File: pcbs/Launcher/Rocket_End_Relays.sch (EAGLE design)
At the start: 40 parts, among them IC2 LM2576T-ADJ, K4 LD105, K5 LD105, K6 LD105, K7 LD105, T1 BC547, T2 BC547, T3 BC547, T4 BC547, T5 BC547, U1 ARDUINO-MEGAPRO-5V, X1 1751248, X2 22-23-2041, X3 22-23-2021, X4 1751248, X5 22-23-2021

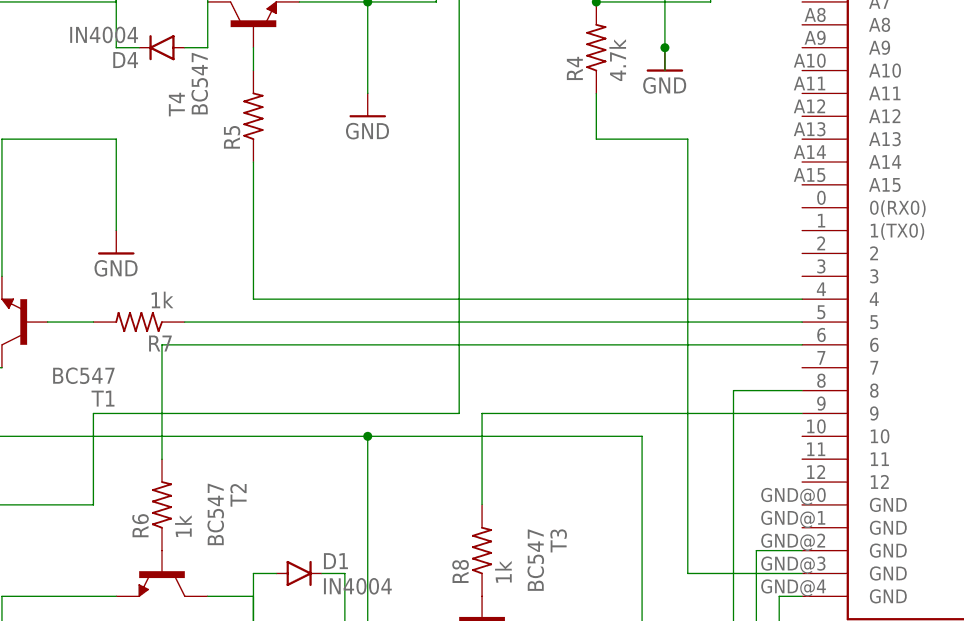
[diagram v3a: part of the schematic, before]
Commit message: * Moving across pins, so we don't use pin 4. Pin 4 is used by SDCARD CS.
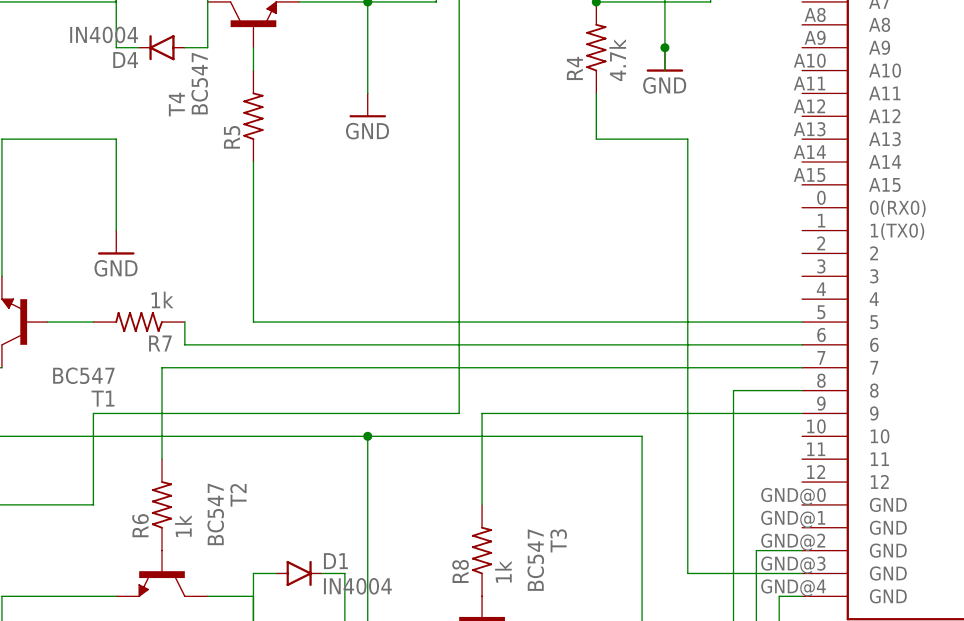
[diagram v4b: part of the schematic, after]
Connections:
- net N$4: now also U1.5; no longer U1.4
- net N$8: now also U1.6; no longer U1.5
- net N$9: now also U1.7; no longer U1.6
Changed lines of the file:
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@@
 <net name="N$4" class="0">
 <segment>
-<pinref part="U1" gate="G$1" pin="4"/>
-<wire x1="17.78" y1="35.56" x2="-43.18" y2="35.56" width="0.1524" layer="91"/>
-<wire x1="-43.18" y1="35.56" x2="-43.18" y2="50.8" width="0.1524" layer="91"/>
+<wire x1="-43.18" y1="33.02" x2="-43.18" y2="50.8" width="0.1524" layer="91"/>
 <pinref part="R5" gate="G$1" pin="1"/>
-</segment>
-</net>
-<net name="N$8" class="0">
-<segment>
 <pinref part="U1" gate="G$1" pin="5"/>
-<wire x1="17.78" y1="33.02" x2="-50.8" y2="33.02" width="0.1524" layer="91"/>
-<pinref part="R7" gate="G$1" pin="1"/>
+<wire x1="-43.18" y1="33.02" x2="17.78" y2="33.02" width="0.1524" layer="91"/>
 </segment>
 </net>
 <net name="N$9" class="0">
 <segment>
-<pinref part="U1" gate="G$1" pin="6"/>
-<wire x1="17.78" y1="30.48" x2="-53.34" y2="30.48" width="0.1524" layer="91"/>
-<wire x1="-53.34" y1="30.48" x2="-53.34" y2="17.78" width="0.1524" layer="91"/>
 <pinref part="R6" gate="G$1" pin="2"/>
+<pinref part="U1" gate="G$1" pin="7"/>
+<wire x1="-53.34" y1="27.94" x2="-53.34" y2="17.78" width="0.1524" layer="91"/>
+<wire x1="17.78" y1="27.94" x2="-53.34" y2="27.94" width="0.1524" layer="91"/>
 </segment>
 </net>
@@
 </segment>
 </net>
+<net name="N$8" class="0">
+<segment>
+<pinref part="R7" gate="G$1" pin="1"/>
+<wire x1="-50.8" y1="33.02" x2="-50.8" y2="30.48" width="0.1524" layer="91"/>
+<pinref part="U1" gate="G$1" pin="6"/>
+<wire x1="-50.8" y1="30.48" x2="17.78" y2="30.48" width="0.1524" layer="91"/>
+</segment>
+</net>

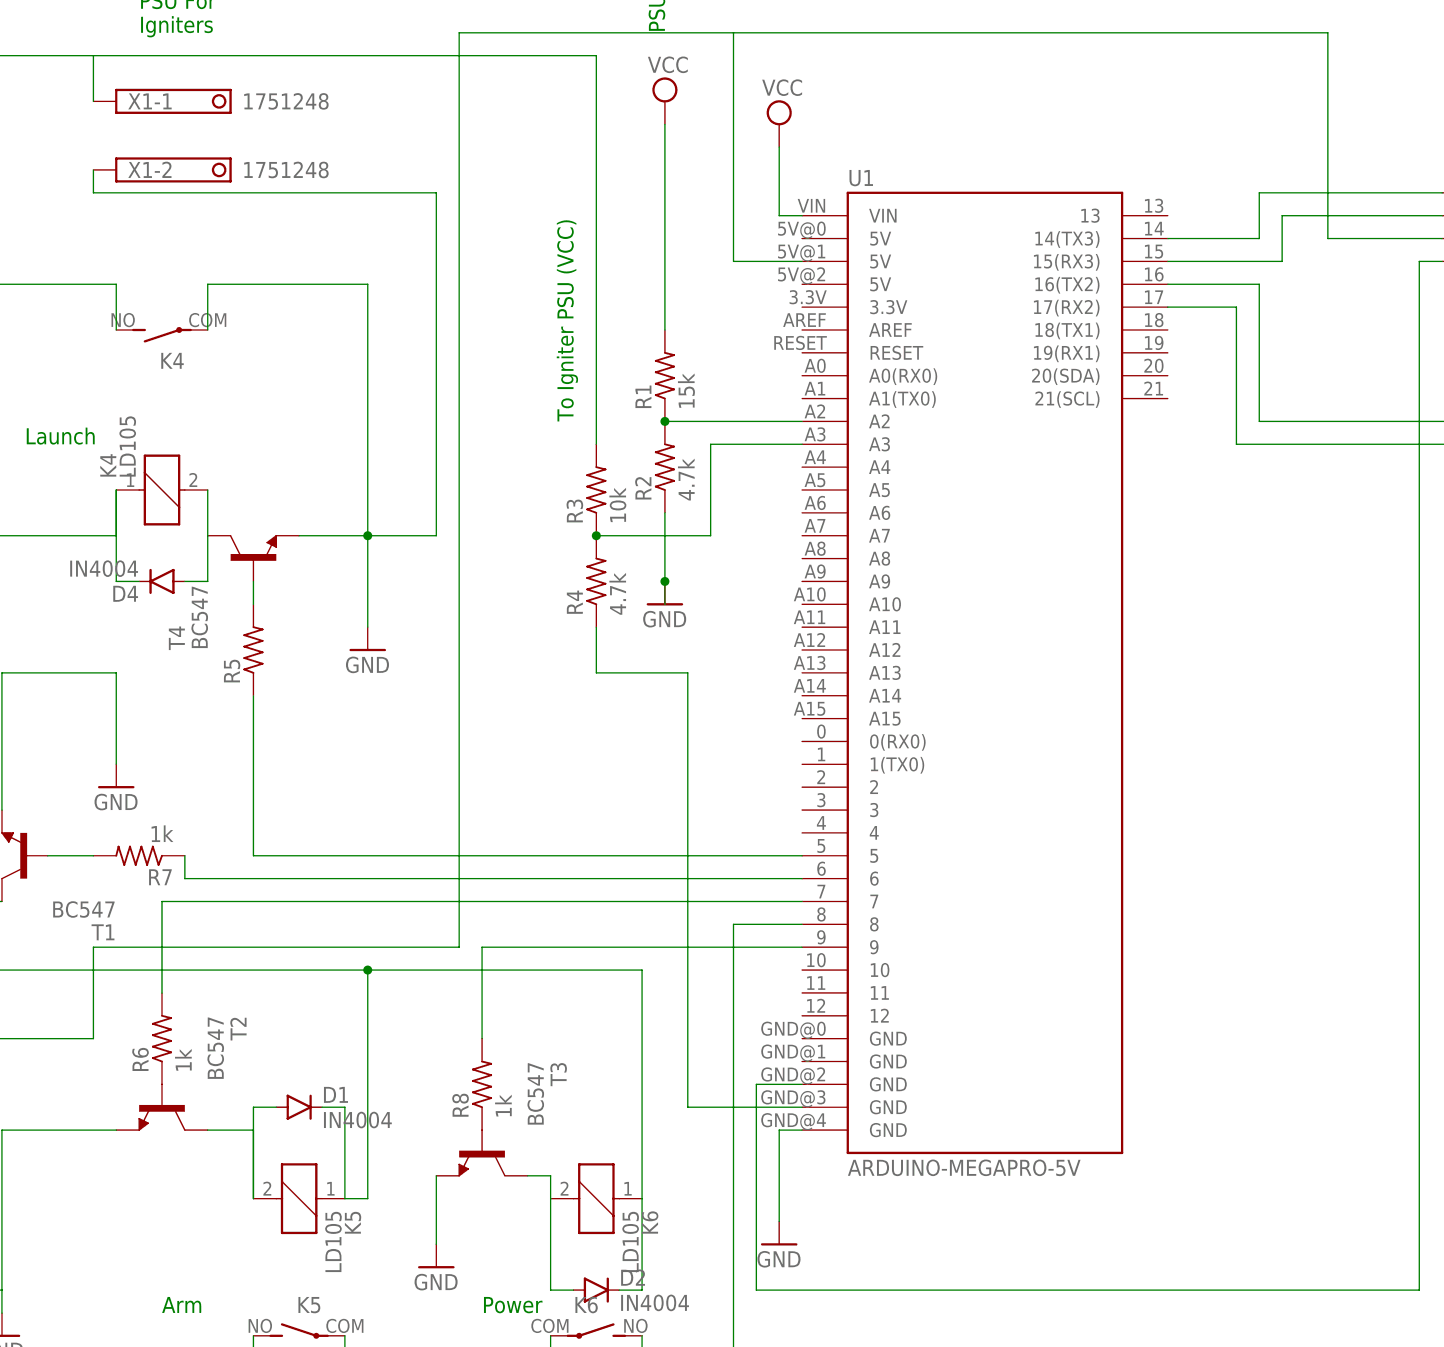
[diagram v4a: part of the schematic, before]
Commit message: * Re-route launch pin to pin 3 instead and keep all other pins as they were.
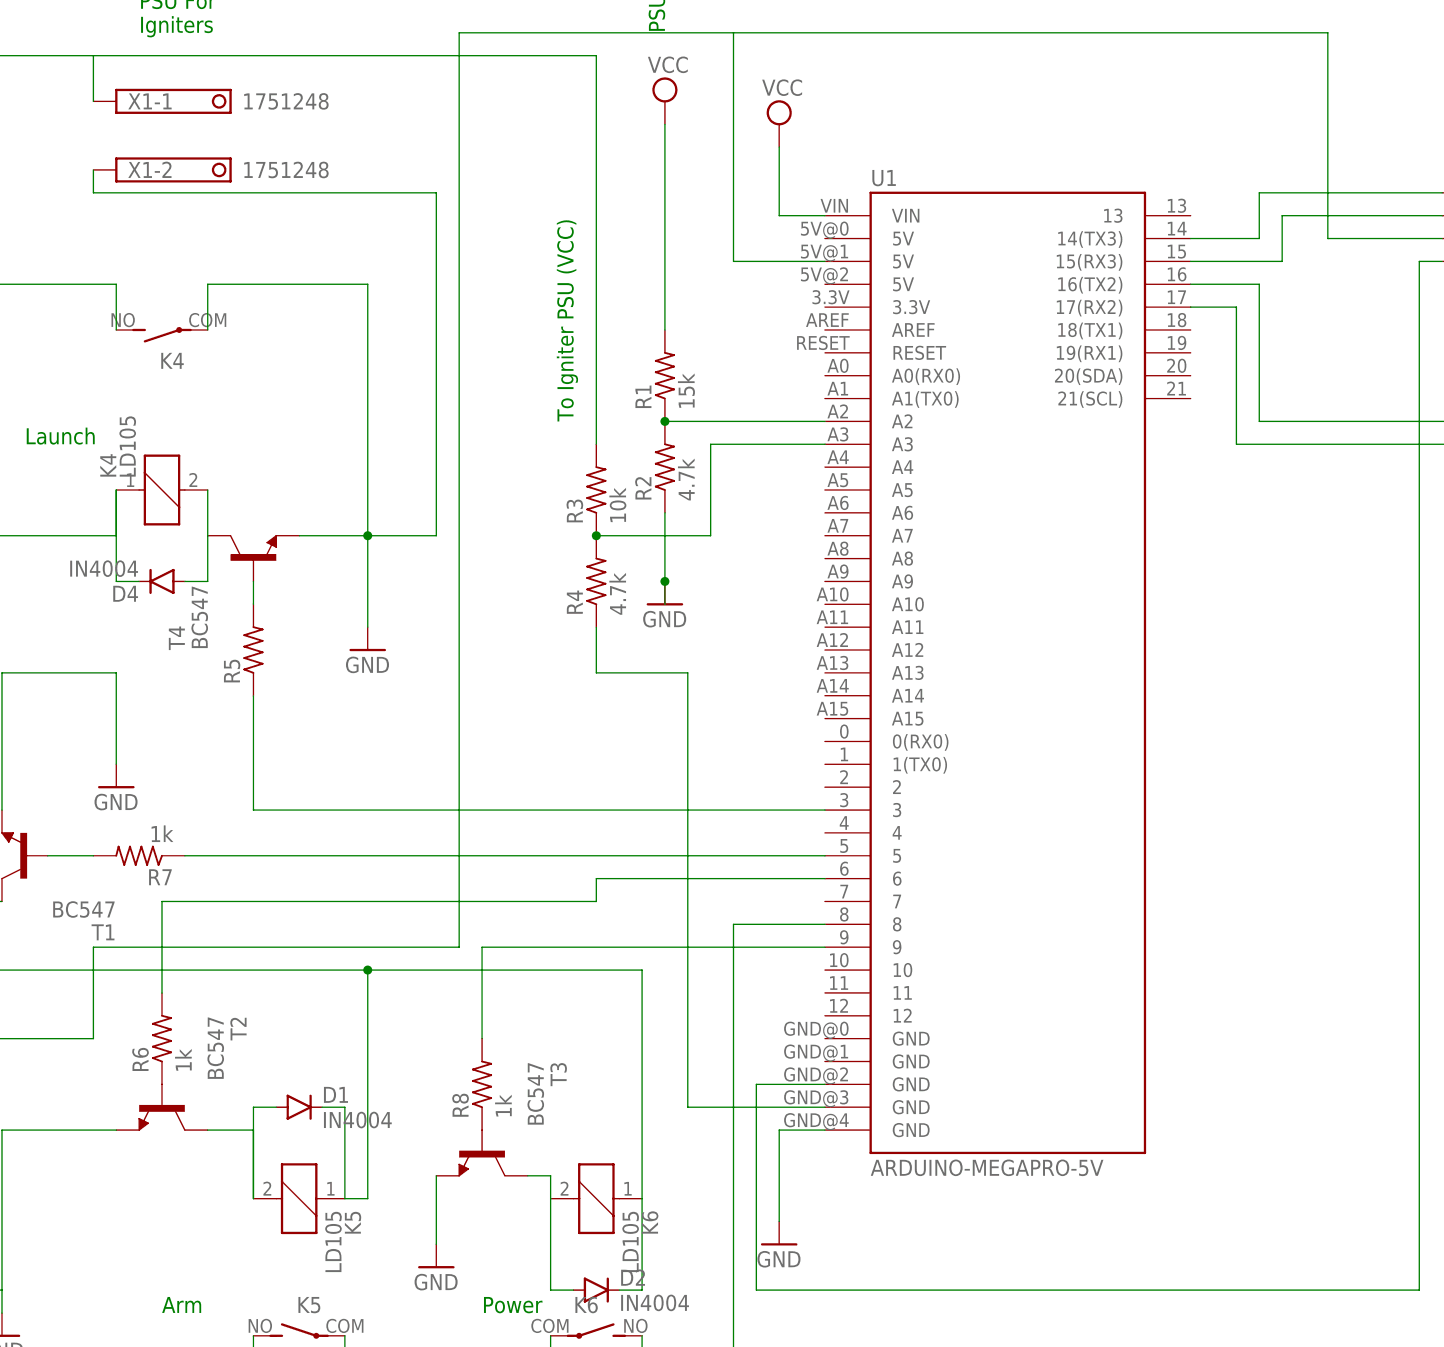
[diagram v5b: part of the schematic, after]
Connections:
- net N$4: now also R7.1; no longer R5.1
- net N$8: now also R5.1, U1.3; no longer R7.1, U1.6
- net N$9: now also U1.6; no longer U1.7
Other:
- moved on the sheet: U1
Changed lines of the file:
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@@
 </plain>
 <instances>
-<instance part="U1" gate="G$1" x="38.1" y="53.34"/>
+<instance part="U1" gate="G$1" x="40.64" y="53.34"/>
 <instance part="X2" gate="-1" x="91.44" y="106.68"/>
 <instance part="X2" gate="-2" x="91.44" y="104.14"/>
@@
 <pinref part="U1" gate="G$1" pin="14(TX3)"/>
 <wire x1="68.58" y1="106.68" x2="68.58" y2="101.6" width="0.1524" layer="91"/>
-<wire x1="68.58" y1="101.6" x2="58.42" y2="101.6" width="0.1524" layer="91"/>
+<wire x1="68.58" y1="101.6" x2="60.96" y2="101.6" width="0.1524" layer="91"/>
 </segment>
 </net>
@@
 <segment>
 <pinref part="U1" gate="G$1" pin="GND@4"/>
-<wire x1="17.78" y1="2.54" x2="15.24" y2="2.54" width="0.1524" layer="91"/>
+<wire x1="20.32" y1="2.54" x2="15.24" y2="2.54" width="0.1524" layer="91"/>
 <wire x1="15.24" y1="2.54" x2="15.24" y2="-7.62" width="0.1524" layer="91"/>
 <pinref part="GND10" gate="1" pin="GND"/>
@@
 <segment>
 <pinref part="U1" gate="G$1" pin="VIN"/>
-<wire x1="17.78" y1="104.14" x2="15.24" y2="104.14" width="0.1524" layer="91"/>
+<wire x1="20.32" y1="104.14" x2="15.24" y2="104.14" width="0.1524" layer="91"/>
 <wire x1="15.24" y1="104.14" x2="15.24" y2="111.76" width="0.1524" layer="91"/>
 <pinref part="SUPPLY3" gate="G$1" pin="VCC"/>
@@
 <segment>
 <pinref part="U1" gate="G$1" pin="A2"/>
-<wire x1="17.78" y1="81.28" x2="2.54" y2="81.28" width="0.1524" layer="91"/>
+<wire x1="20.32" y1="81.28" x2="2.54" y2="81.28" width="0.1524" layer="91"/>
 <pinref part="R1" gate="G$1" pin="1"/>
 <pinref part="R2" gate="G$1" pin="2"/>
@@
 <segment>
 <pinref part="U1" gate="G$1" pin="A3"/>
-<wire x1="17.78" y1="78.74" x2="7.62" y2="78.74" width="0.1524" layer="91"/>
+<wire x1="20.32" y1="78.74" x2="7.62" y2="78.74" width="0.1524" layer="91"/>
 <wire x1="7.62" y1="78.74" x2="7.62" y2="68.58" width="0.1524" layer="91"/>
 <wire x1="7.62" y1="68.58" x2="-5.08" y2="68.58" width="0.1524" layer="91"/>
@@
 </segment>
 </net>
-<net name="N$4" class="0">
-<segment>
-<wire x1="-43.18" y1="33.02" x2="-43.18" y2="50.8" width="0.1524" layer="91"/>
-<pinref part="R5" gate="G$1" pin="1"/>
-<pinref part="U1" gate="G$1" pin="5"/>
-<wire x1="-43.18" y1="33.02" x2="17.78" y2="33.02" width="0.1524" layer="91"/>
-</segment>
-</net>
 <net name="N$9" class="0">
 <segment>
 <pinref part="R6" gate="G$1" pin="2"/>
-<pinref part="U1" gate="G$1" pin="7"/>
 <wire x1="-53.34" y1="27.94" x2="-53.34" y2="17.78" width="0.1524" layer="91"/>
-<wire x1="17.78" y1="27.94" x2="-53.34" y2="27.94" width="0.1524" layer="91"/>
+<wire x1="-53.34" y1="27.94" x2="-5.08" y2="27.94" width="0.1524" layer="91"/>
+<wire x1="-5.08" y1="27.94" x2="-5.08" y2="30.48" width="0.1524" layer="91"/>
+<wire x1="-5.08" y1="30.48" x2="20.32" y2="30.48" width="0.1524" layer="91"/>
+<pinref part="U1" gate="G$1" pin="6"/>
 </segment>
 </net>
@@
 <segment>
 <pinref part="U1" gate="G$1" pin="8"/>
-<wire x1="17.78" y1="25.4" x2="10.16" y2="25.4" width="0.1524" layer="91"/>
+<wire x1="20.32" y1="25.4" x2="10.16" y2="25.4" width="0.1524" layer="91"/>
 <wire x1="10.16" y1="25.4" x2="10.16" y2="-43.18" width="0.1524" layer="91"/>
 <pinref part="T5" gate="G$1" pin="C"/>
@@
 <pinref part="U1" gate="G$1" pin="16(TX2)"/>
 <wire x1="68.58" y1="81.28" x2="68.58" y2="96.52" width="0.1524" layer="91"/>
-<wire x1="68.58" y1="96.52" x2="58.42" y2="96.52" width="0.1524" layer="91"/>
+<wire x1="68.58" y1="96.52" x2="60.96" y2="96.52" width="0.1524" layer="91"/>
 <pinref part="JP1" gate="G$1" pin="4"/>
 <wire x1="68.58" y1="81.28" x2="91.44" y2="81.28" width="0.1524" layer="91"/>
@@
 <segment>
 <pinref part="U1" gate="G$1" pin="17(RX2)"/>
-<wire x1="58.42" y1="93.98" x2="66.04" y2="93.98" width="0.1524" layer="91"/>
+<wire x1="60.96" y1="93.98" x2="66.04" y2="93.98" width="0.1524" layer="91"/>
 <wire x1="66.04" y1="93.98" x2="66.04" y2="78.74" width="0.1524" layer="91"/>
 <pinref part="JP1" gate="G$1" pin="5"/>
@@
 <segment>
 <pinref part="U1" gate="G$1" pin="9"/>
-<wire x1="17.78" y1="22.86" x2="-17.78" y2="22.86" width="0.1524" layer="91"/>
+<wire x1="20.32" y1="22.86" x2="-17.78" y2="22.86" width="0.1524" layer="91"/>
 <pinref part="R8" gate="G$1" pin="2"/>
 <wire x1="-17.78" y1="22.86" x2="-17.78" y2="12.7" width="0.1524" layer="91"/>
@@
 <segment>
 <pinref part="U1" gate="G$1" pin="15(RX3)"/>
-<wire x1="71.12" y1="99.06" x2="58.42" y2="99.06" width="0.1524" layer="91"/>
+<wire x1="71.12" y1="99.06" x2="60.96" y2="99.06" width="0.1524" layer="91"/>
 <wire x1="71.12" y1="99.06" x2="71.12" y2="104.14" width="0.1524" layer="91"/>
 <pinref part="X2" gate="-2" pin="S"/>
@@
 <wire x1="86.36" y1="-15.24" x2="12.7" y2="-15.24" width="0.1524" layer="91"/>
 <wire x1="12.7" y1="-15.24" x2="12.7" y2="7.62" width="0.1524" layer="91"/>
-<wire x1="12.7" y1="7.62" x2="17.78" y2="7.62" width="0.1524" layer="91"/>
+<wire x1="12.7" y1="7.62" x2="20.32" y2="7.62" width="0.1524" layer="91"/>
 <pinref part="U1" gate="G$1" pin="GND@2"/>
 </segment>
@@
 <wire x1="5.08" y1="53.34" x2="5.08" y2="5.08" width="0.1524" layer="91"/>
 <pinref part="U1" gate="G$1" pin="GND@3"/>
-<wire x1="5.08" y1="5.08" x2="17.78" y2="5.08" width="0.1524" layer="91"/>
+<wire x1="5.08" y1="5.08" x2="20.32" y2="5.08" width="0.1524" layer="91"/>
 </segment>
 </net>
@@
 <wire x1="10.16" y1="124.46" x2="76.2" y2="124.46" width="0.1524" layer="91"/>
 <pinref part="U1" gate="G$1" pin="5V@1"/>
-<wire x1="17.78" y1="99.06" x2="10.16" y2="99.06" width="0.1524" layer="91"/>
+<wire x1="20.32" y1="99.06" x2="10.16" y2="99.06" width="0.1524" layer="91"/>
 <wire x1="-20.32" y1="124.46" x2="10.16" y2="124.46" width="0.1524" layer="91"/>
 </segment>
@@
 </segment>
 </net>
+<net name="N$4" class="0">
+<segment>
+<pinref part="R7" gate="G$1" pin="1"/>
+<pinref part="U1" gate="G$1" pin="5"/>
+<wire x1="-50.8" y1="33.02" x2="20.32" y2="33.02" width="0.1524" layer="91"/>
+</segment>
+</net>
 <net name="N$8" class="0">
 <segment>
-<pinref part="R7" gate="G$1" pin="1"/>
-<wire x1="-50.8" y1="33.02" x2="-50.8" y2="30.48" width="0.1524" layer="91"/>
-<pinref part="U1" gate="G$1" pin="6"/>
-<wire x1="-50.8" y1="30.48" x2="17.78" y2="30.48" width="0.1524" layer="91"/>
-</segment>
-</net>
+<pinref part="R5" gate="G$1" pin="1"/>
+<wire x1="-43.18" y1="50.8" x2="-43.18" y2="38.1" width="0.1524" layer="91"/>
+<pinref part="U1" gate="G$1" pin="3"/>
+<wire x1="-43.18" y1="38.1" x2="20.32" y2="38.1" width="0.1524" layer="91"/>
+</segment>
+</net>

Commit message: * Lots of adjustments to track to deal with issues that EaglePCB finds.
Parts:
- R11: device rcl:R-US_0204/7 -> resistor:R-US_0207/12
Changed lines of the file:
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@@
 <part name="GND6" library="supply1" deviceset="GND" device=""/>
 <part name="R9" library="rcl" deviceset="R-US_" device="0204/7" value="10k"/>
-<part name="R11" library="rcl" deviceset="R-US_" device="0204/7" value="1k"/>
+<part name="R11" library="resistor" deviceset="R-US_" device="0207/12" value="1k"/>
 <part name="T5" library="transistor" deviceset="BC547" device=""/>
 <part name="R12" library="resistor" deviceset="R-US_" device="0204/7" value="10k"/>
@@
 </segment>
 </net>
-<net name="N$25" class="0">
+<net name="N$28" class="0">
 <segment>
 <wire x1="-10.16" y1="-27.94" x2="-10.16" y2="-20.32" width="0.1524" layer="91"/>
